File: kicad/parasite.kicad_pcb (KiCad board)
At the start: 2 copper layers, 22 x 126.4 mm, 31 parts, among them Q1 MMBT3906, Q4 Q_Photo_NPN, SW1 B3U-1000P, U1 E73-2G4M08S1C, U2 SHTC3, Y1 32.768kHz

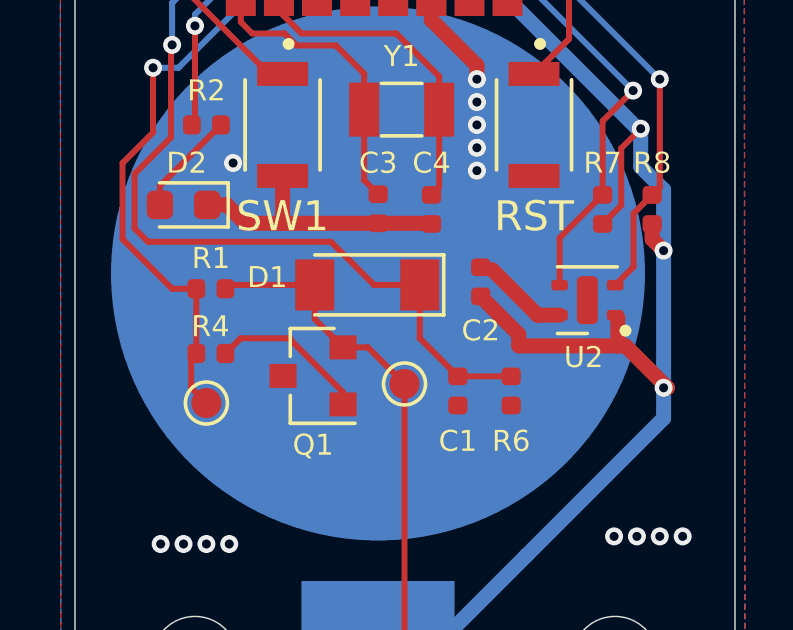
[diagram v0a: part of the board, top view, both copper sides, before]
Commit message: Diode Footprint changed
Changed LL4148 to the 1N4148 variant, soldering preference.
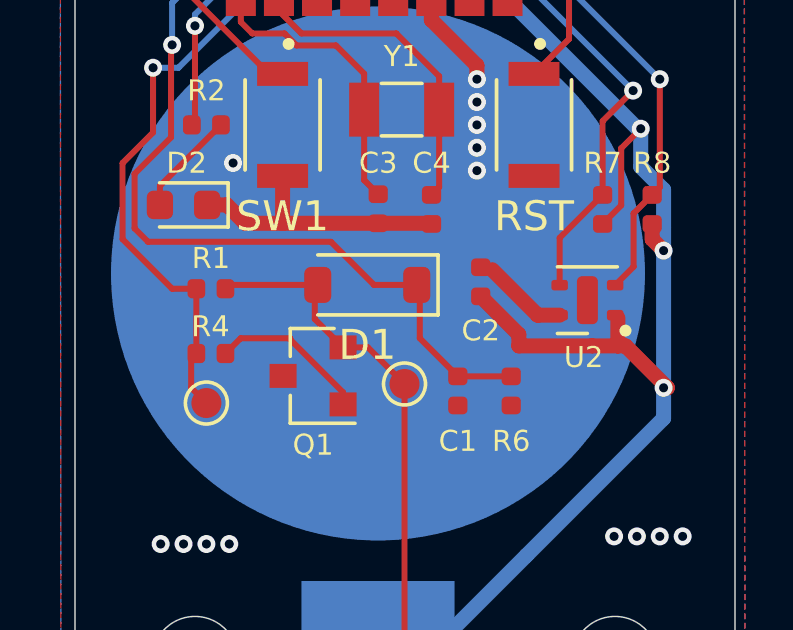
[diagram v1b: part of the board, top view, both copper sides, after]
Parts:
- D1: footprint Diode_SMD:D_MiniMELF -> Diode_SMD:D_SOD-123
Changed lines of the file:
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@@
       (plot_on_all_layers_selection 0x0000000_00000000)
       (disableapertmacros false)
-      (usegerberextensions false)
+      (usegerberextensions true)
       (usegerberattributes false)
       (usegerberadvancedattributes false)
@@
       (psa4output false)
       (plotreference true)
-      (plotvalue true)
+      (plotvalue false)
       (plotinvisibletext false)
       (sketchpadsonfab false)
-      (subtractmaskfromsilk false)
+      (subtractmaskfromsilk true)
       (outputformat 1)
       (mirror false)
@@
     (descr "SOT-23, Standard")
     (tags "SOT-23")
+    (property "LCSC" "C2910191")
     (property "Sheetfile" "parasite.kicad_sch")
     (property "Sheetname" "")
@@
     )
   )
-  (footprint "Diode_SMD:D_MiniMELF" (layer "F.Cu")
+  (footprint "Diode_SMD:D_SOD-123" (layer "F.Cu")
     (at 66.742 55.536 180)
-    (descr "Diode Mini-MELF")
-    (tags "Diode Mini-MELF")
+    (descr "SOD-123")
+    (tags "SOD-123")
     (property "LCSC" "C9808")
     (property "Sheetfile" "parasite.kicad_sch")
@@
     (property "ki_keywords" "diode")
     (attr smd)
-    (fp_text reference "D1" (at 3.33 0.254 180) (layer "F.SilkS")
-        (effects (font (size 0.7 0.7) (thickness 0.12)))
-    )
-    (fp_text value "LL4148" (at 0 1.75) (layer "F.Fab")
-        (effects (font (size 1 1) (thickness 0.15)))
-    )
-    (fp_text user "${REFERENCE}" (at -0.05 0) (layer "F.Fab")
-        (effects (font (size 0.7 0.7) (thickness 0.12)))
-    )
-    (fp_line (start -2.55 -1) (end -2.55 1)
-      (stroke (width 0.12) (type solid)) (layer "F.SilkS"))
-    (fp_line (start -2.55 1) (end 1.75 1)
-      (stroke (width 0.12) (type solid)) (layer "F.SilkS"))
-    (fp_line (start 1.75 -1) (end -2.55 -1)
-      (stroke (width 0.12) (type solid)) (layer "F.SilkS"))
-    (fp_line (start -2.65 -1.1) (end 2.65 -1.1)
-      (stroke (width 0.05) (type solid)) (layer "F.CrtYd"))
-    (fp_line (start -2.65 1.1) (end -2.65 -1.1)
-      (stroke (width 0.05) (type solid)) (layer "F.CrtYd"))
-    (fp_line (start 2.65 -1.1) (end 2.65 1.1)
-      (stroke (width 0.05) (type solid)) (layer "F.CrtYd"))
-    (fp_line (start 2.65 1.1) (end -2.65 1.1)
-      (stroke (width 0.05) (type solid)) (layer "F.CrtYd"))
-    (fp_line (start -1.65 -0.8) (end 1.65 -0.8)
-      (stroke (width 0.1) (type solid)) (layer "F.Fab"))
-    (fp_line (start -1.65 0.8) (end -1.65 -0.8)
+    (fp_text reference "D1" (at 0 -2 180) (layer "F.SilkS")
+        (effects (font (size 1 1) (thickness 0.15)))
+    )
+    (fp_text value "LL4148" (at 0 2.1 180) (layer "F.Fab")
+        (effects (font (size 1 1) (thickness 0.15)))
+    )
+    (fp_text user "${REFERENCE}" (at 0 -2 180) (layer "F.Fab")
+        (effects (font (size 1 1) (thickness 0.15)))
+    )
+    (fp_line (start -2.36 -1) (end -2.36 1)
+      (stroke (width 0.12) (type solid)) (layer "F.SilkS"))
+    (fp_line (start -2.36 -1) (end 1.65 -1)
+      (stroke (width 0.12) (type solid)) (layer "F.SilkS"))
+    (fp_line (start -2.36 1) (end 1.65 1)
+      (stroke (width 0.12) (type solid)) (layer "F.SilkS"))
+    (fp_line (start -2.35 -1.15) (end -2.35 1.15)
+      (stroke (width 0.05) (type solid)) (layer "F.CrtYd"))
+    (fp_line (start -2.35 -1.15) (end 2.35 -1.15)
+      (stroke (width 0.05) (type solid)) (layer "F.CrtYd"))
+    (fp_line (start 2.35 -1.15) (end 2.35 1.15)
+      (stroke (width 0.05) (type solid)) (layer "F.CrtYd"))
+    (fp_line (start 2.35 1.15) (end -2.35 1.15)
+      (stroke (width 0.05) (type solid)) (layer "F.CrtYd"))
+    (fp_line (start -1.4 -0.9) (end 1.4 -0.9)
+      (stroke (width 0.1) (type solid)) (layer "F.Fab"))
+    (fp_line (start -1.4 0.9) (end -1.4 -0.9)
       (stroke (width 0.1) (type solid)) (layer "F.Fab"))
     (fp_line (start -0.75 0) (end -0.35 0)
@@
     (fp_line (start 0.25 0.4) (end -0.35 0)
       (stroke (width 0.1) (type solid)) (layer "F.Fab"))
-    (fp_line (start 1.65 -0.8) (end 1.65 0.8)
-      (stroke (width 0.1) (type solid)) (layer "F.Fab"))
-    (fp_line (start 1.65 0.8) (end -1.65 0.8)
-      (stroke (width 0.1) (type solid)) (layer "F.Fab"))
-    (pad "1" smd rect (at -1.75 0 180) (size 1.3 1.7) (layers "F.Cu" "F.Paste" "F.Mask")
+    (fp_line (start 1.4 -0.9) (end 1.4 0.9)
+      (stroke (width 0.1) (type solid)) (layer "F.Fab"))
+    (fp_line (start 1.4 0.9) (end -1.4 0.9)
+      (stroke (width 0.1) (type solid)) (layer "F.Fab"))
+    (pad "1" smd roundrect (at -1.65 0 180) (size 0.9 1.2) (layers "F.Cu" "F.Paste" "F.Mask") (roundrect_rratio 0.25)
       (net 2 "SENS_OUT") (pinfunction "K") (pintype "passive"))
-    (pad "2" smd rect (at 1.75 0 180) (size 1.3 1.7) (layers "F.Cu" "F.Paste" "F.Mask")
+    (pad "2" smd roundrect (at 1.65 0 180) (size 0.9 1.2) (layers "F.Cu" "F.Paste" "F.Mask") (roundrect_rratio 0.25)
       (net 7 "CPARA") (pinfunction "A") (pintype "passive"))
-    (model "${KISYS3DMOD}/Diode_SMD.3dshapes/D_MiniMELF.wrl"
-      (offset (xyz 0 0 0))
-      (scale (xyz 1 1 1))
+    (model "${KICAD6_3DMODEL_DIR}/Diode_SMD.3dshapes/D_SOD-123.wrl"
+      (offset (xyz 0 0 0))
+      (scale (xyz 1 1 1))

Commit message: Updated PCB and BOM
Updated PCB and BOM to reflect new diode value
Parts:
- D1: value LL4148 -> 1N4148W
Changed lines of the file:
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@@
         (effects (font (size 1 1) (thickness 0.15)))
     )
-    (fp_text value "LL4148" (at 0 2.1 180) (layer "F.Fab")
+    (fp_text value "1N4148W" (at 0 2.1 180) (layer "F.Fab")
         (effects (font (size 1 1) (thickness 0.15)))
     )

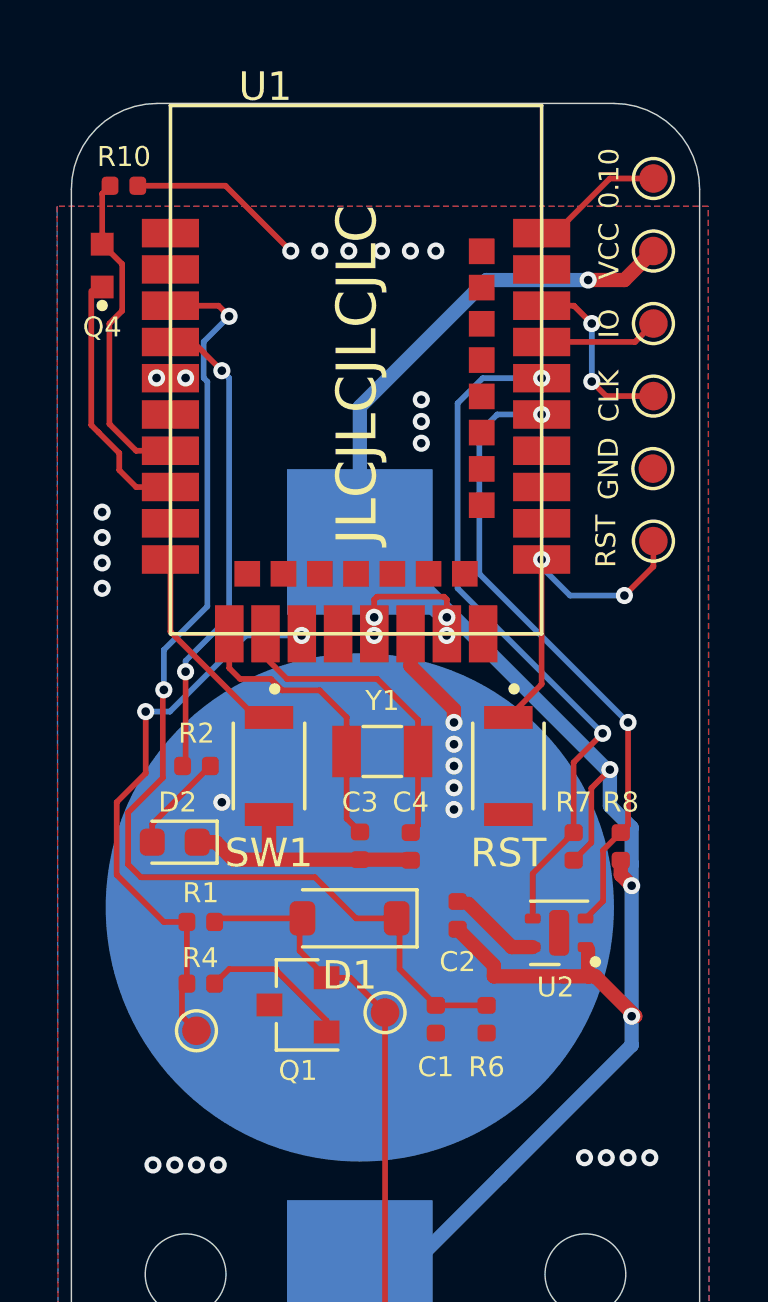
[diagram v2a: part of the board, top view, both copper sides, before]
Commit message: Replaced Footprints
Replaced all 0402 footprints with 0805, moved around the routing and parts to create space.
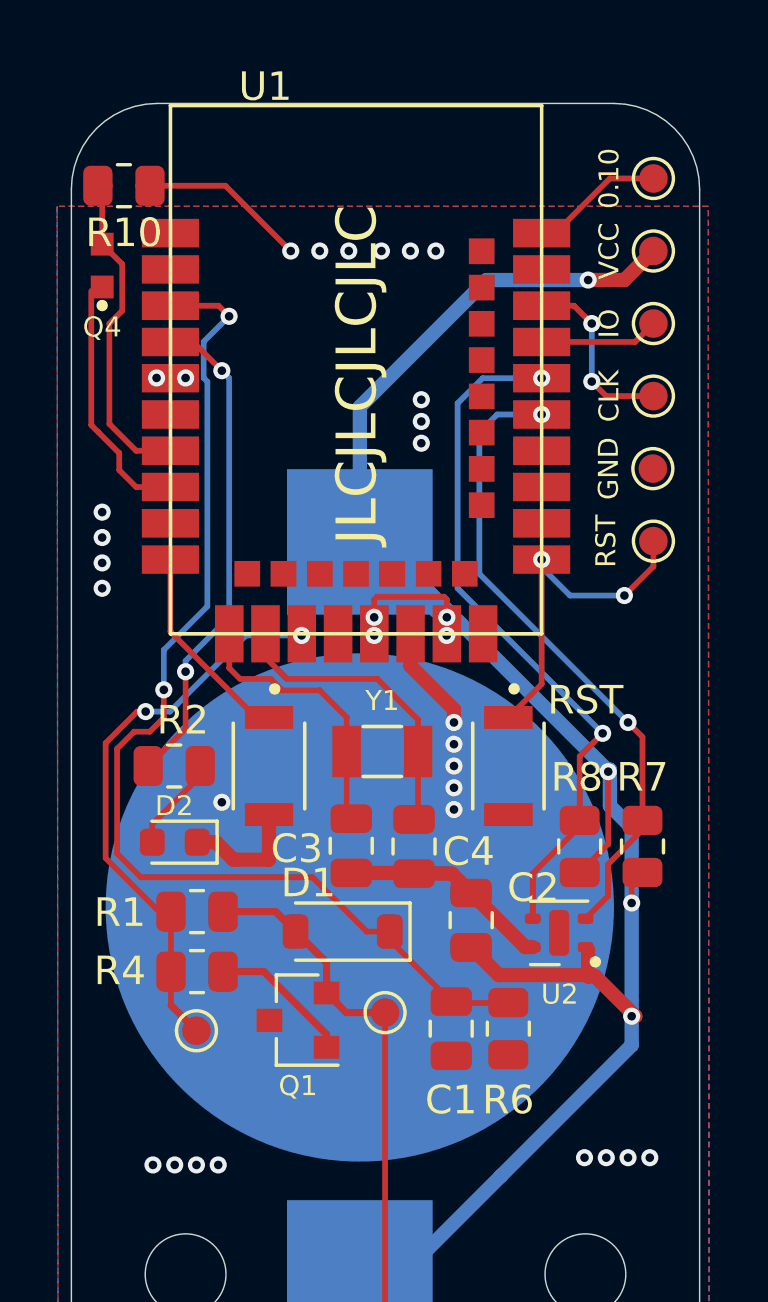
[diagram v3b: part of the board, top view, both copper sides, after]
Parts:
- C1, C2, C3, C4: footprint Capacitor_SMD:C_0402_1005Metric -> Capacitor_SMD:C_0805_2012Metric
- R1, R10, R2, R4, R6, R7, R8: footprint Resistor_SMD:R_0402_1005Metric -> Resistor_SMD:R_0805_2012Metric
- moved R6 0.83 mm to (72.3, 59.4)
- moved R2 0.78 mm to (60.6, 50.2)
- moved R8 0.76 mm to (77.0, 53.0)
- moved C1 0.63 mm to (70.3, 59.4)
- moved Q1 0.53 mm to (64.9, 59.1)
- moved D1 0.52 mm to (66.5, 56.0)
- moved C2 0.50 mm to (71.0, 55.6)
- moved R4 0.44 mm to (61.4, 57.4)
- moved R1 0.39 mm to (61.4, 55.3)
- moved C3 0.31 mm to (66.8, 53.0)
- moved R7 0.21 mm to (74.8, 53.0)
- moved C4 0.12 mm to (69.0, 53.0)
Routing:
- net SENS_OUT: track 38.5 -> 39.3 mm
- net Net-(U1B-P0.00/XL1): track 10.2 -> 9.64 mm
- net Net-(U1B-P0.01/XL2): track 11.1 -> 10.6 mm
- net LED: track 16.9 -> 17.4 mm
